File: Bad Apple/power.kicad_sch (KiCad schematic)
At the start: 0 parts

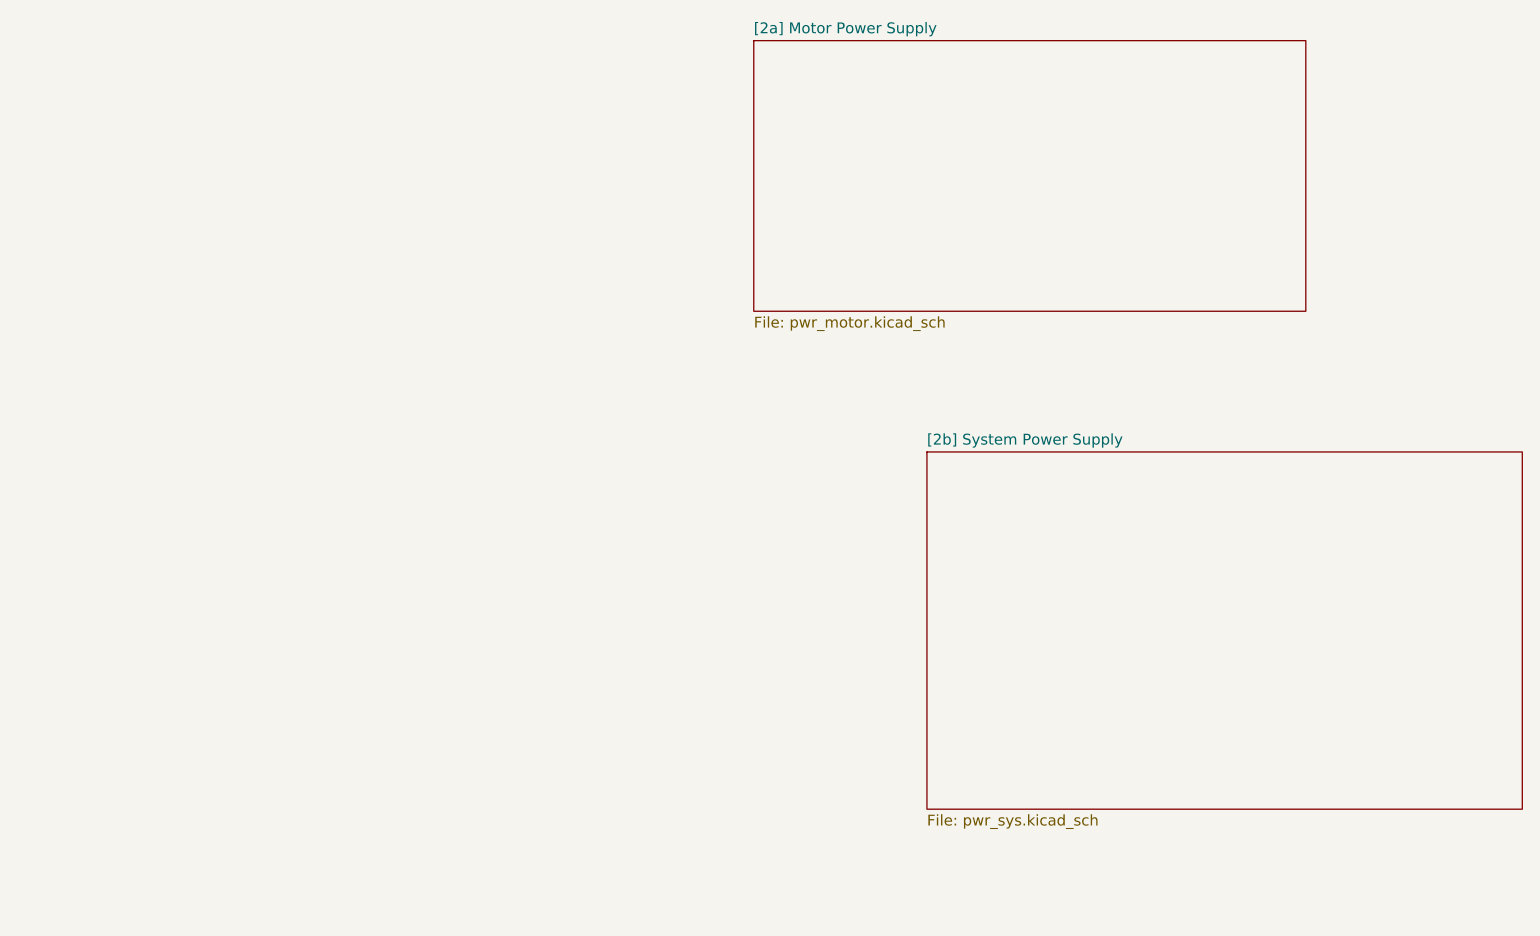
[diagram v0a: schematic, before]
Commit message: feat(pcb): more hierarchy
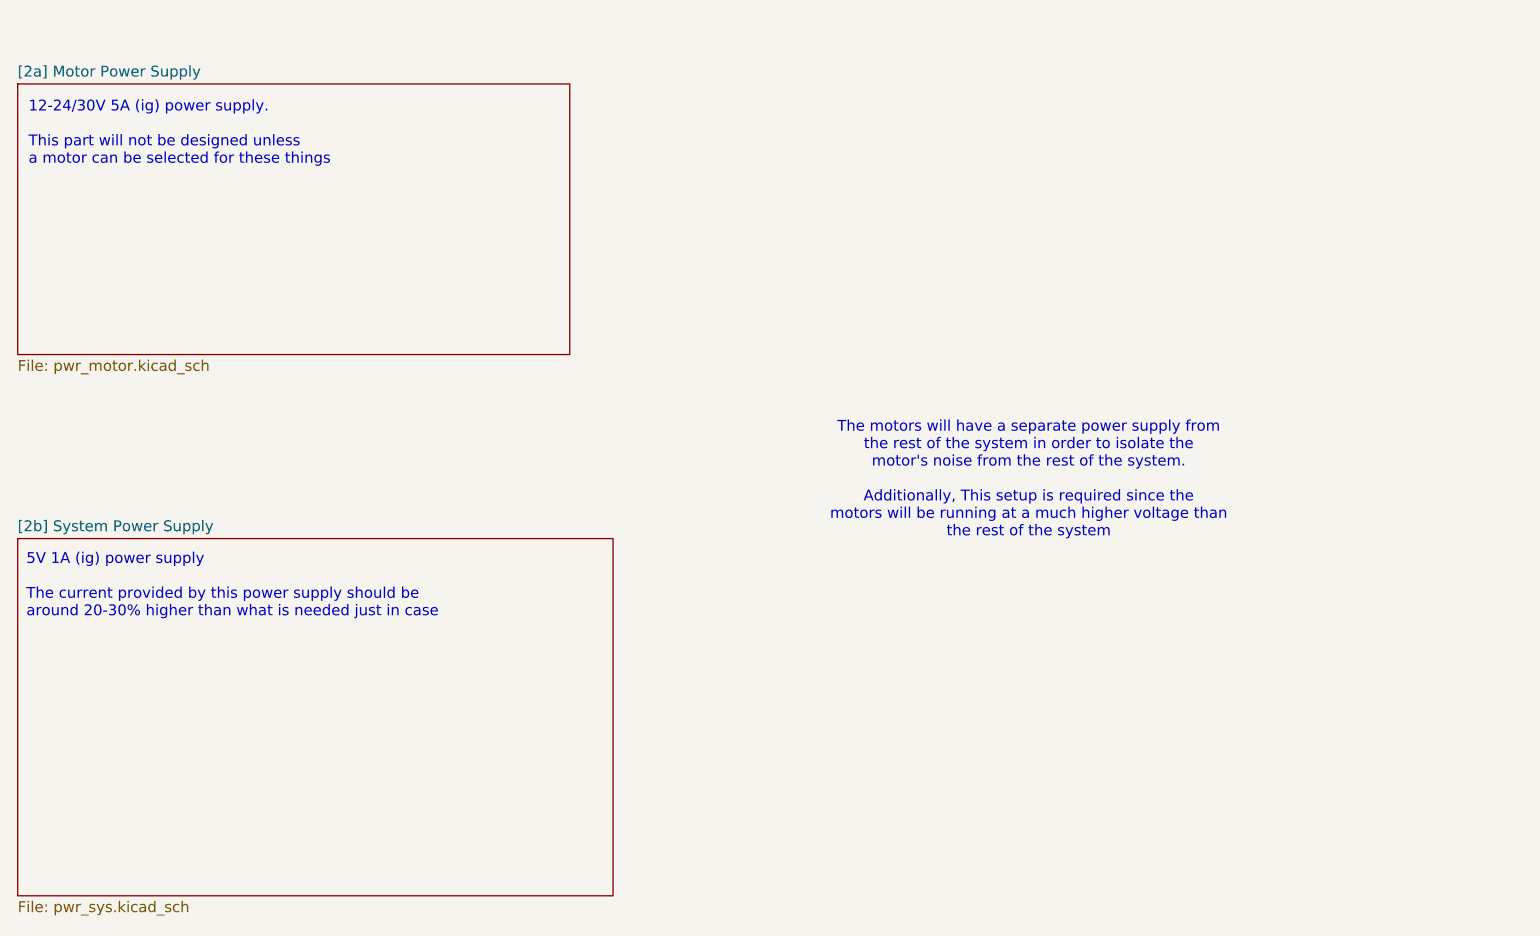
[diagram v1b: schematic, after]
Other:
- note added: "12-24/30V 5A (ig) power supply. This part will not be designed unless a motor can be selected for these things"
- note added: "5V 1A (ig) power supply The current provided by this power supply should be around 20-30% higher than what is needed just in case"
- note added: "The motors will have a separate power supply from the rest of the system in order to isolate the motor's noise from the rest of the system. Additionally, This setup is required since the motors will be running at a much higher voltage than the rest of the system"
- company: (none) -> Mixed Engineering Group 3 | STEM 12-Altruism / AY 2526 | CIT-U SHS
- title: (none) -> Autonomous  Courier Robot "Bad Apple"
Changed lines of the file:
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@@
 	(generator_version "9.0")
 	(paper "A4")
+	(title_block
+		(title "Autonomous  Courier Robot \"Bad Apple\"")
+		(date "2025-08-28")
+		(rev "1")
+		(company "Mixed Engineering Group 3 | STEM 12-Altruism / AY 2526 | CIT-U SHS")
+	)
+	(text "12-24/30V 5A (ig) power supply.\n\nThis part will not be designed unless\na motor can be selected for these things"
+		(exclude_from_sim no)
+		(at 58.42 37.592 0)
+		(effects
+			(font
+				(size 1.27 1.27)
+			)
+			(justify left)
+		)
+	)
+	(text "5V 1A (ig) power supply\n\nThe current provided by this power supply should be\naround 20-30% higher than what is needed just in case"
+		(exclude_from_sim no)
+		(at 58.166 90.678 0)
+		(effects
+			(font
+				(size 1.27 1.27)
+			)
+			(justify left)
+		)
+	)
+	(text "The motors will have a separate power supply from\nthe rest of the system in order to isolate the\nmotor's noise from the rest of the system.\n\nAdditionally, This setup is required since the\nmotors will be running at a much higher voltage than\nthe rest of the system"
+		(exclude_from_sim no)
+		(at 175.768 78.232 0)
+		(effects
+			(font
+				(size 1.27 1.27)
+			)
+		)
+	)
 	(sheet
-		(at 143.51 26.67)
+		(at 57.15 31.75)
 		(size 64.77 31.75)
 		(exclude_from_sim no)
@@
 		)
 		(property "Sheetname" "[2a] Motor Power Supply"
-			(at 143.51 25.9584 0)
+			(at 57.15 31.0384 0)
 			(effects
 				(font
@@
 		)
 		(property "Sheetfile" "pwr_motor.kicad_sch"
-			(at 143.51 59.0046 0)
+			(at 57.15 64.0846 0)
 			(effects
 				(font
@@
 	)
 	(sheet
-		(at 163.83 74.93)
+		(at 57.15 85.09)
 		(size 69.85 41.91)
 		(exclude_from_sim no)
@@
 		)
 		(property "Sheetname" "[2b] System Power Supply"
-			(at 163.83 74.2184 0)
+			(at 57.15 84.3784 0)
 			(effects
 				(font
@@
 		)
 		(property "Sheetfile" "pwr_sys.kicad_sch"
-			(at 163.83 117.4246 0)
+			(at 57.15 127.5846 0)
 			(effects
 				(font
